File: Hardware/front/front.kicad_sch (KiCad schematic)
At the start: 20 parts

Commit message: More rework of controller
- Updated power section to use a transformer + DC/DC modules, rather
  than a switching AC/DC supply: this should result in fewer bits of
  random noise floating around

- Moved a bunch of stuff around, and changed pinouts slightly of
  external connectors

- Start work on removing dependency on rear IO board

- Minor tweaks to part numbers on front panel board
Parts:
- U: MPN 875105142005 -> A768EB107M1ELAE036
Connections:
- net GND: now also J.6 (Pin_6)
- net at J.1 (Pin_1), J.2 (Pin_2), J.3 (Pin_3)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: now also J.5 (Pin_5)
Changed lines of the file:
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@@
   (junction (at 101.6 66.675) (diameter 0) (color 0 0 0 0)
   )
+  (junction (at 128.905 81.915) (diameter 0) (color 0 0 0 0)
+  )
   (junction (at 109.855 71.755) (diameter 0) (color 0 0 0 0)
   )
@@
   )
   (junction (at 150.495 237.49) (diameter 0) (color 0 0 0 0)
+  )
+  (junction (at 128.905 74.295) (diameter 0) (color 0 0 0 0)
   )
   (junction (at 109.855 112.395) (diameter 0) (color 0 0 0 0)
@@
     (stroke (width 0) (type default))
   )
+  (wire (pts (xy 128.905 79.375) (xy 128.905 81.915))
+    (stroke (width 0) (type default))
+  )
   (bus (pts (xy 116.205 117.475) (xy 116.205 120.015))
     (stroke (width 0) (type default))
@@
   )
   (wire (pts (xy 128.905 97.155) (xy 109.855 97.155))
+    (stroke (width 0) (type default))
+  )
+  (wire (pts (xy 128.905 74.295) (xy 128.905 76.835))
     (stroke (width 0) (type default))
   )
@@
       (effects (font (size 1.27 1.27)) hide)
     )
-    (property "MPN" "875105142005" (id 4) (at 107.315 69.215 0)
+    (property "MPN" "A768EB107M1ELAE036" (id 4) (at 107.315 69.215 0)
       (effects (font (size 1.27 1.27)) hide)
     )
@@
     )
     (path "/b368bb56-368c-4656-aee8-6b29ed3a76c2"
-      (reference "C102") (unit 1) (value "100µF") (footprint "Capacitor_SMD:CP_Elec_5x5.3")
+      (reference "C102") (unit 1) (value "100µF") (footprint "Capacitor_SMD:CP_Elec_6.3x5.7")
     )
     (path "/aa09bac2-00c0-43cd-8de4-3e18d20d4a7e"

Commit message: More reworking of the controller and friends
- Add more rear IO to the controller, in this case finishing positioning
  of the Ethernet jack, and adding a suitable right angle USB B jack
  (USB C is preferrable but there's basically no jacks that are
  sufficiently long)

- Mostly finish power section on controller (save for the enable input
  for our +3V3 rail; it'll be slaved off the SoM +3V3 rail)

- Minor tweaks to pinout of FFC connector on front panel

- Update cutout shape of analog board

- Fixed a few footprints metadata

- Add footprints for further rear panel IO
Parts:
- removed U: (no value), symbol Connector_Generic:Conn_02x10_Odd_Even
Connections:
- net ENCODER_A: now also J.7 (Pin_7)
- net ENCODER_B: now also J.6 (Pin_6)
- net GND: now also J.5 (Pin_5); no longer J.6 (Pin_6), J.7 (Pin_7)
- net at J.1 (Pin_1), J.2 (Pin_2), J.3 (Pin_3)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: no longer J.5 (Pin_5)
- no-connect marks 10 -> 3
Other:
- note removed: "To Controller Board"

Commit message: Start routing front panel stuff
- Routed some of the LED driver pins and replaced footprints of passives
  with 0603 size to match the controller board
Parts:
- U: MPN CL21B104KACNFNC -> (none)
- U: MPN A768EB107M1ELAE036 -> A768EB336M1GLAE045
- U: MPN RMC1/10-103JTP -> (none)
- U: MPN RC0805FR-132KL -> (none)
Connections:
- net LED_EN_R: no longer U.14 (LED7)
- net LED_MENU: now also U.14 (LED7); no longer U.15 (LED8)
- net LED_MODE_EXT: now also U.20 (LED12); no longer U.8 (LED2)
- net LED_STATUS_B: now also U.16 (LED9); no longer U.6 (LED0)
- net LED_STATUS_G: now also U.15 (LED8); no longer U.16 (LED9)
- net LED_STATUS_R: now also U.17 (LED10); no longer U.7 (LED1)
- net LED_TRIGGER: now also U.18 (LED11); no longer U.20 (LED12)
- no-connect marks 3 -> 1
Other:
- note added: "TODO: pull up RESET, SPI ~{CS}"

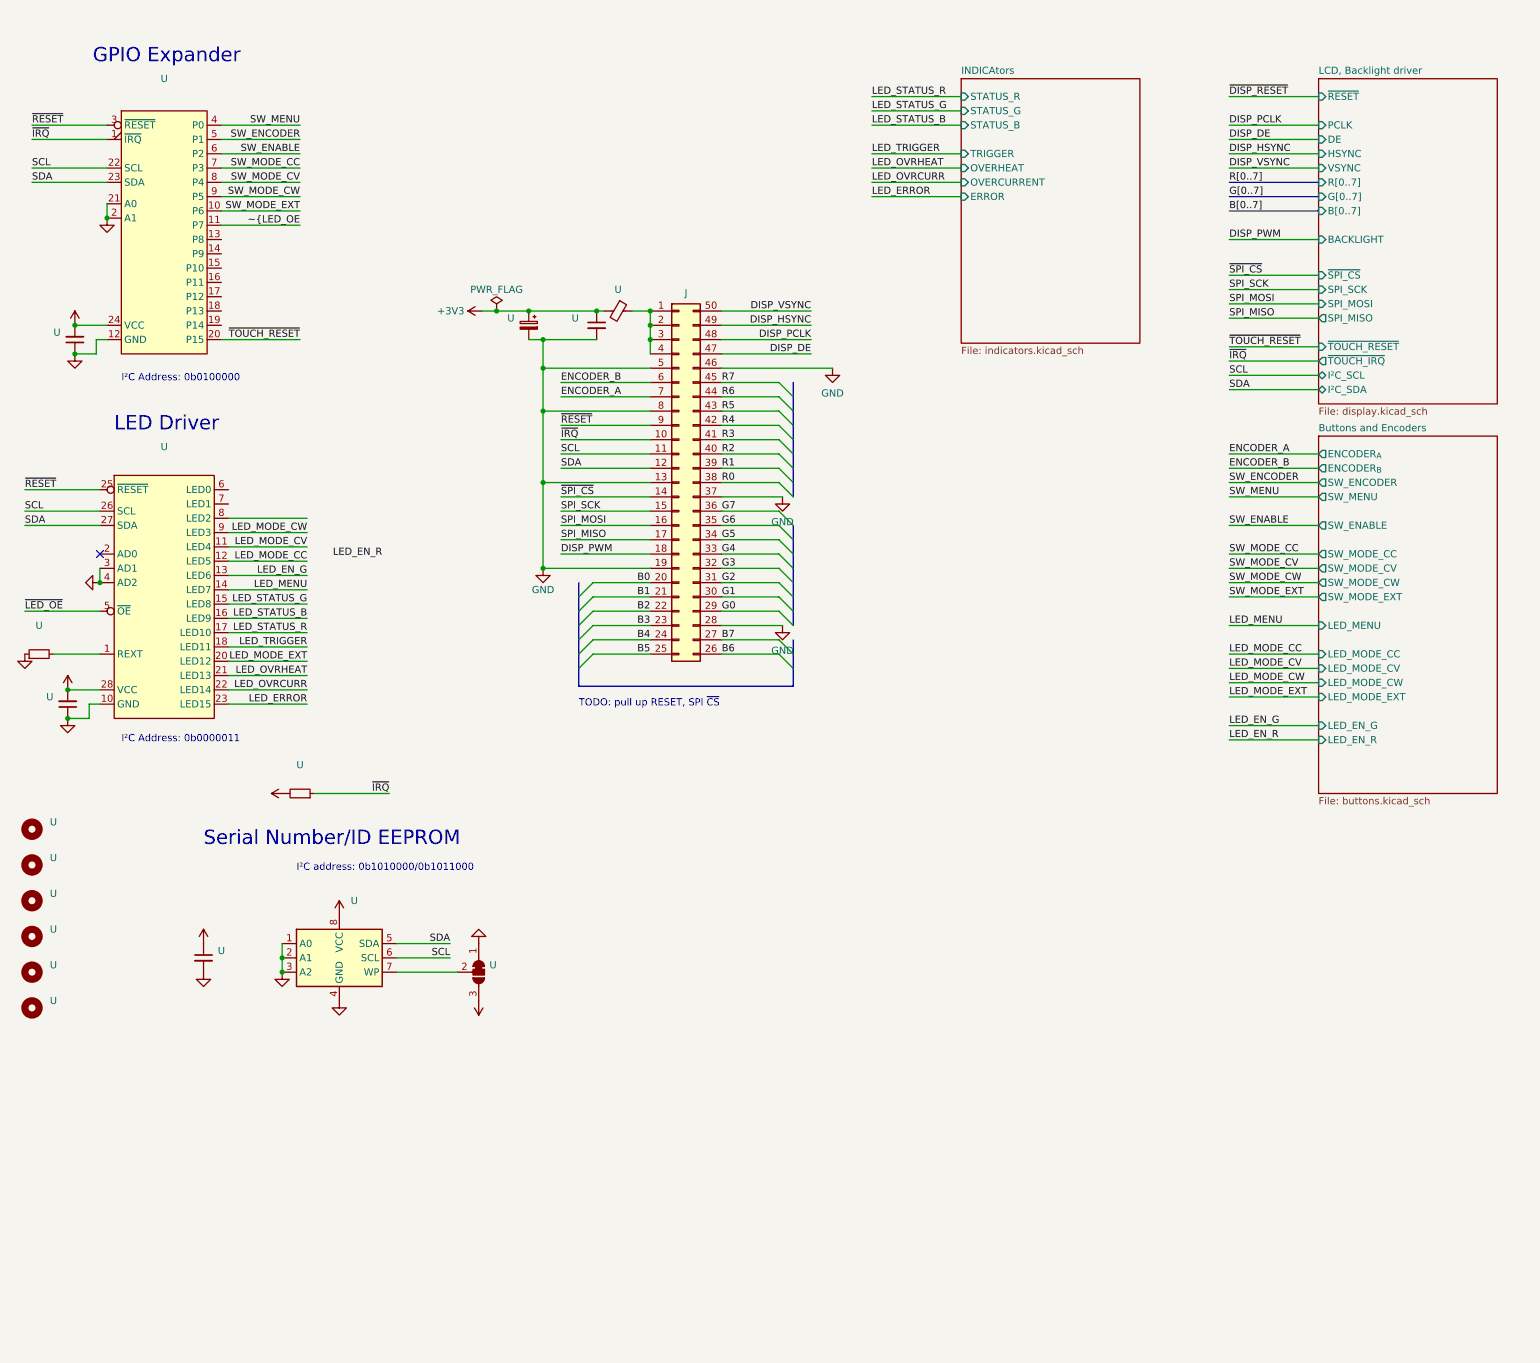
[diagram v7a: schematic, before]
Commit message: Finished routing front panel
- Finished routing the contents of the front panel; it could probably
  use an optimization pass and general cleanup.

  A few of the assignments of IOs/LED driver outputs were changed as
  well to make the routing less of a pain in the ass, as compared to the
  previous front panels.

- Minor tweaks to controller to remove some unused signals
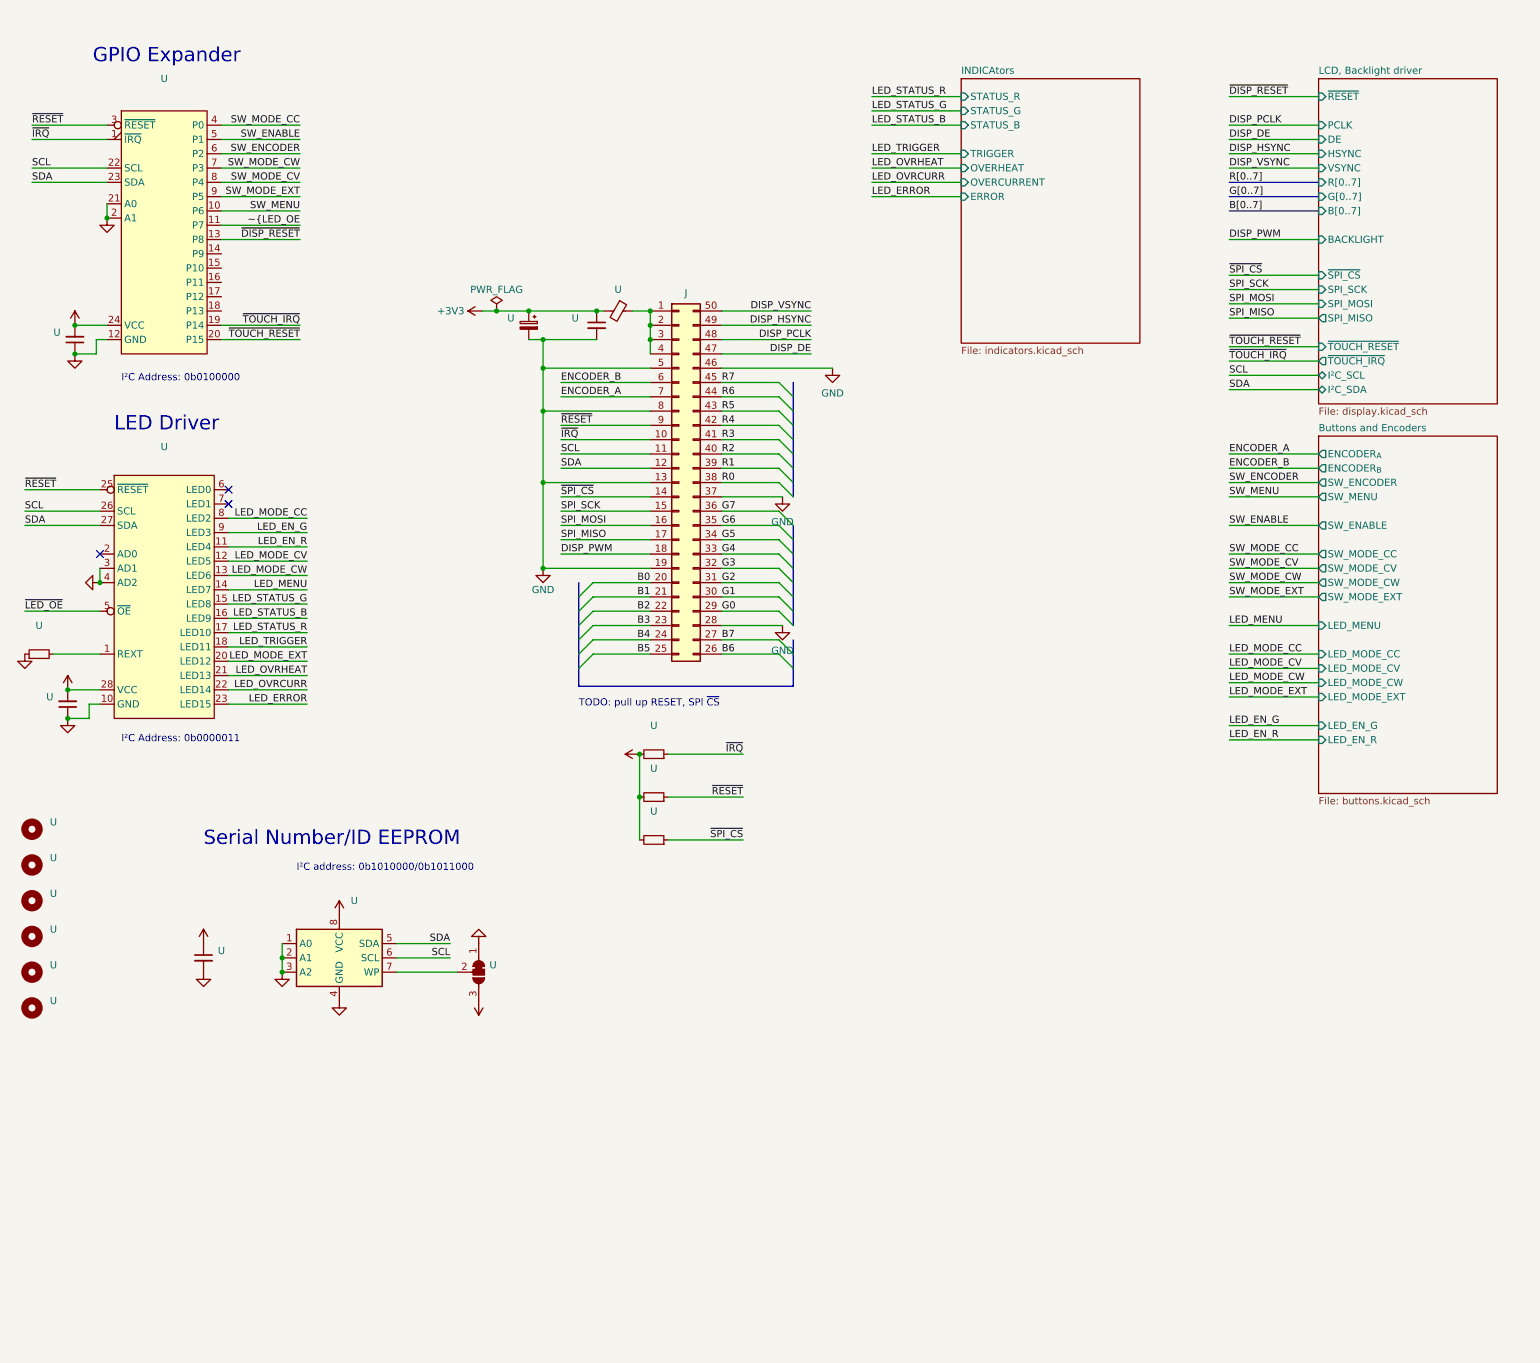
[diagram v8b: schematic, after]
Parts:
- added U (x2): (no value), symbol Device:R_Small
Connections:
- net +3V3: now also U.2, U.2
- net LED_EN_G: now also U.9 (LED3); no longer U.13 (LED6)
- net LED_EN_R: now also U.11 (LED4)
- net LED_MODE_CC: now also U.8 (LED2); no longer U.12 (LED5)
- net LED_MODE_CV: now also U.12 (LED5); no longer U.11 (LED4)
- net LED_MODE_CW: now also U.13 (LED6); no longer U.9 (LED3)
- net SW_ENABLE: now also U.5 (P1); no longer U.6 (P2)
- net SW_ENCODER: now also U.6 (P2); no longer U.5 (P1)
- net SW_MENU: now also U.10 (P6); no longer U.4 (P0)
- net SW_MODE_CC: now also U.4 (P0); no longer U.7 (P3)
- net SW_MODE_CW: now also U.7 (P3); no longer U.9 (P5)
- net SW_MODE_EXT: now also U.9 (P5); no longer U.10 (P6)
- net ~{DISP_RESET}: now also U.13 (P8)
- net ~{RESET}: now also U.1
- net ~{SPI_CS}: now also U.1
- net ~{TOUCH_IRQ}: now reaches U.19 (P14)
- no-connect marks 1 -> 3
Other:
- moved on the sheet: U
